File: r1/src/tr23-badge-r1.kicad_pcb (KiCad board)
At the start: 4 copper layers, 111.2 x 142.3 mm, 249 parts, among them J1 532610271, J2 USB-C-12, J3 USB-A-10mm-flangeless, J4 AFC07-S40ECA-00, J5 PJ-320D, J6 2x03-socket-2.54-through-board, J7 TF-15x15, J8 DNP, Q1 MMBT3904-TP, Q2 MMBT3904-TP, Q3 MMBT3904-TP, Q4 DMG2305UX-13, Q5 DMG2305UX-13, Q6 AP2302B, SW1 REV_TACT, SW10 REV_TACT, SW11 REV_TACT, SW12 REV_TACT, SW13 REV_TACT, SW14 REV_TACT, SW15 REV_TACT, SW16 REV_TACT, SW17 REV_TACT, SW18 REV_TACT, SW19 REV_TACT, SW2 REV_TACT, SW20 REV_TACT, SW21 REV_TACT, SW22 REV_TACT, SW23 REV_TACT, SW24 REV_TACT, SW25 REV_TACT, SW26 REV_TACT, SW27 REV_TACT, SW28 REV_TACT, SW29 REV_TACT, SW3 REV_TACT, SW30 REV_TACT, SW31 REV_TACT, SW32 REV_TACT, SW33 REV_TACT, SW34 REV_TACT, SW4 REV_TACT, SW5 REV_TACT, SW6 REV_TACT, SW7 REV_TACT, SW8 REV_TACT, SW9 REV_TACT, U1 MCP73831T-2ACI_OT, U2 AP2114H-3_3TRG1, U3 CP2102N-A01-GQFN24, U4 PCM5100APW, U5 PAM8908, U6 PCA9555PW, U7 PCA9555PW, U8 PCA9555PW, U9 CC1200, Y1 32.768kHz, Y2 40Mhz

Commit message: Position audio sectoin
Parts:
- C39, C40: moved to B.Cu
- moved C39 109.1 mm to (17.2, -86.0)
- moved Q6 72.5 mm to (-8.66, -104.1)
- moved C40 70.7 mm to (-21.2, -86.0)
- moved C19 33.2 mm to (-22.4, -109.2), turned to -90 degrees
- moved C13 32.5 mm to (-22.7, -114.6)
- moved C14 31.7 mm to (-16.9, -117.8)
- moved C17 31.7 mm to (-15.7, -118.4)
- moved C15 31.7 mm to (-18.2, -118.4)
- moved C16 31.7 mm to (-20.5, -117.7)
- moved C20 31.7 mm to (-20.1, -107.6)
- moved C22 31.7 mm to (-13.3, -112.3)
- moved C18 31.7 mm to (-21.4, -107.9)
- moved C23 31.7 mm to (-13.3, -110.8)
- moved C24 31.7 mm to (-13.3, -113.8)
- moved U4 31.7 mm to (-18.5, -113.0)
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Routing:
- net /SCL: track 11.6 -> 68.5 mm, vias 3 -> 4
- net /SDA: track 11.4 -> 67.3 mm, vias 4 -> 5
- net /I2S_SD: track 0.00 -> 21.7 mm, vias 0 -> 2
- net /I2S_WS: track 3.26 -> 23.6 mm, vias 0 -> 2
- net +3.3V: track 56.8 -> 67.1 mm, vias 17 -> 19
- net /audio/DAC_OUTL: track 0.00 -> 6.84 mm
- net /audio/DAC_OUTR: track 0.00 -> 5.16 mm
- net Net-(U5-INR-): track 0.00 -> 2.36 mm
- net Net-(U5-INL-): track 0.00 -> 2.30 mm
- net /I2S_SCK: track 0.00 -> 2.13 mm, vias 0 -> 1
- net Net-(U4-CAPP): track 0.00 -> 1.98 mm
- net Net-(U4-VNEG): track 0.00 -> 1.95 mm
- net Net-(U4-CAPM): track 0.00 -> 1.87 mm
- net /AMP_GAIN0: track 0.00 -> 1.76 mm, vias 0 -> 1
- net /audio/OUTR: track 0.00 -> 1.65 mm, vias 0 -> 1
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
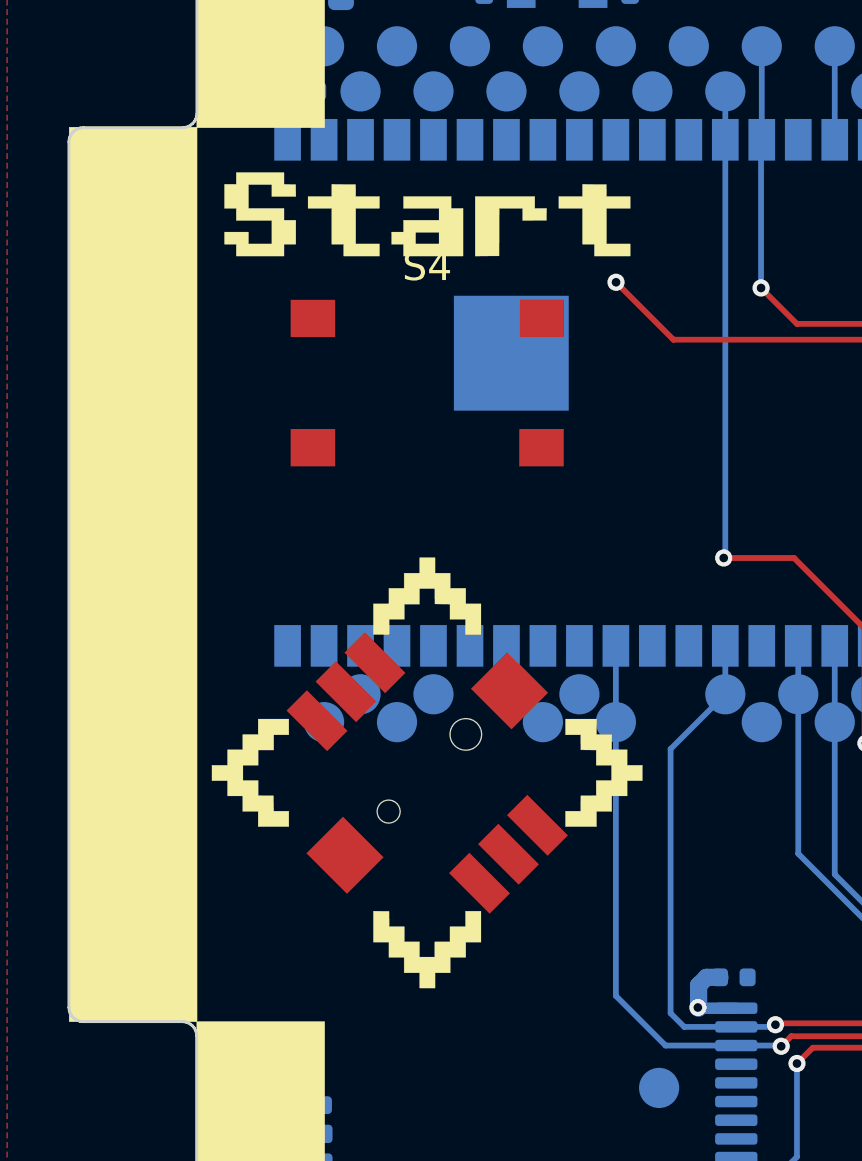
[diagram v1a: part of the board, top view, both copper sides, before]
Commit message: Tweak position of nav and A buttons, and update silk to match
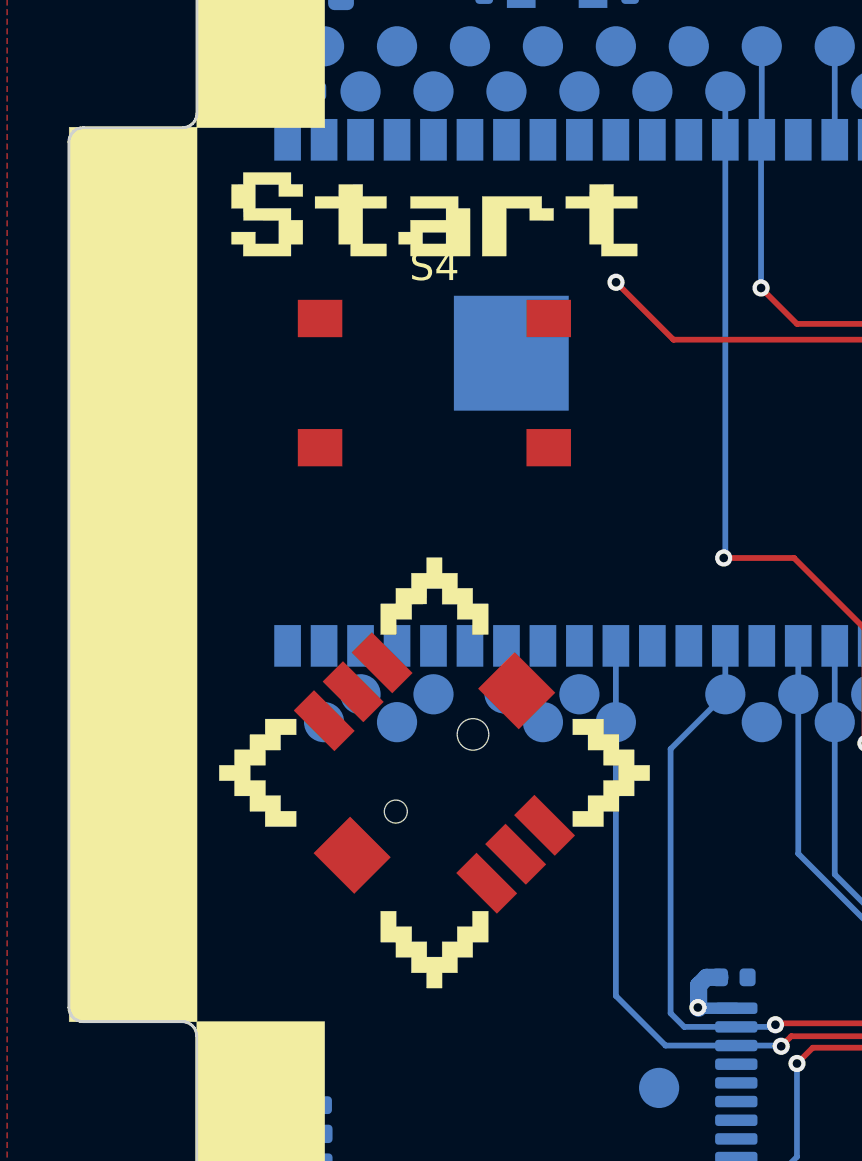
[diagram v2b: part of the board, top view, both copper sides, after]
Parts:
- moved S4 0.25 mm to (-42.9, -106.7)
- moved S5 0.25 mm to (-42.9, -93.2)

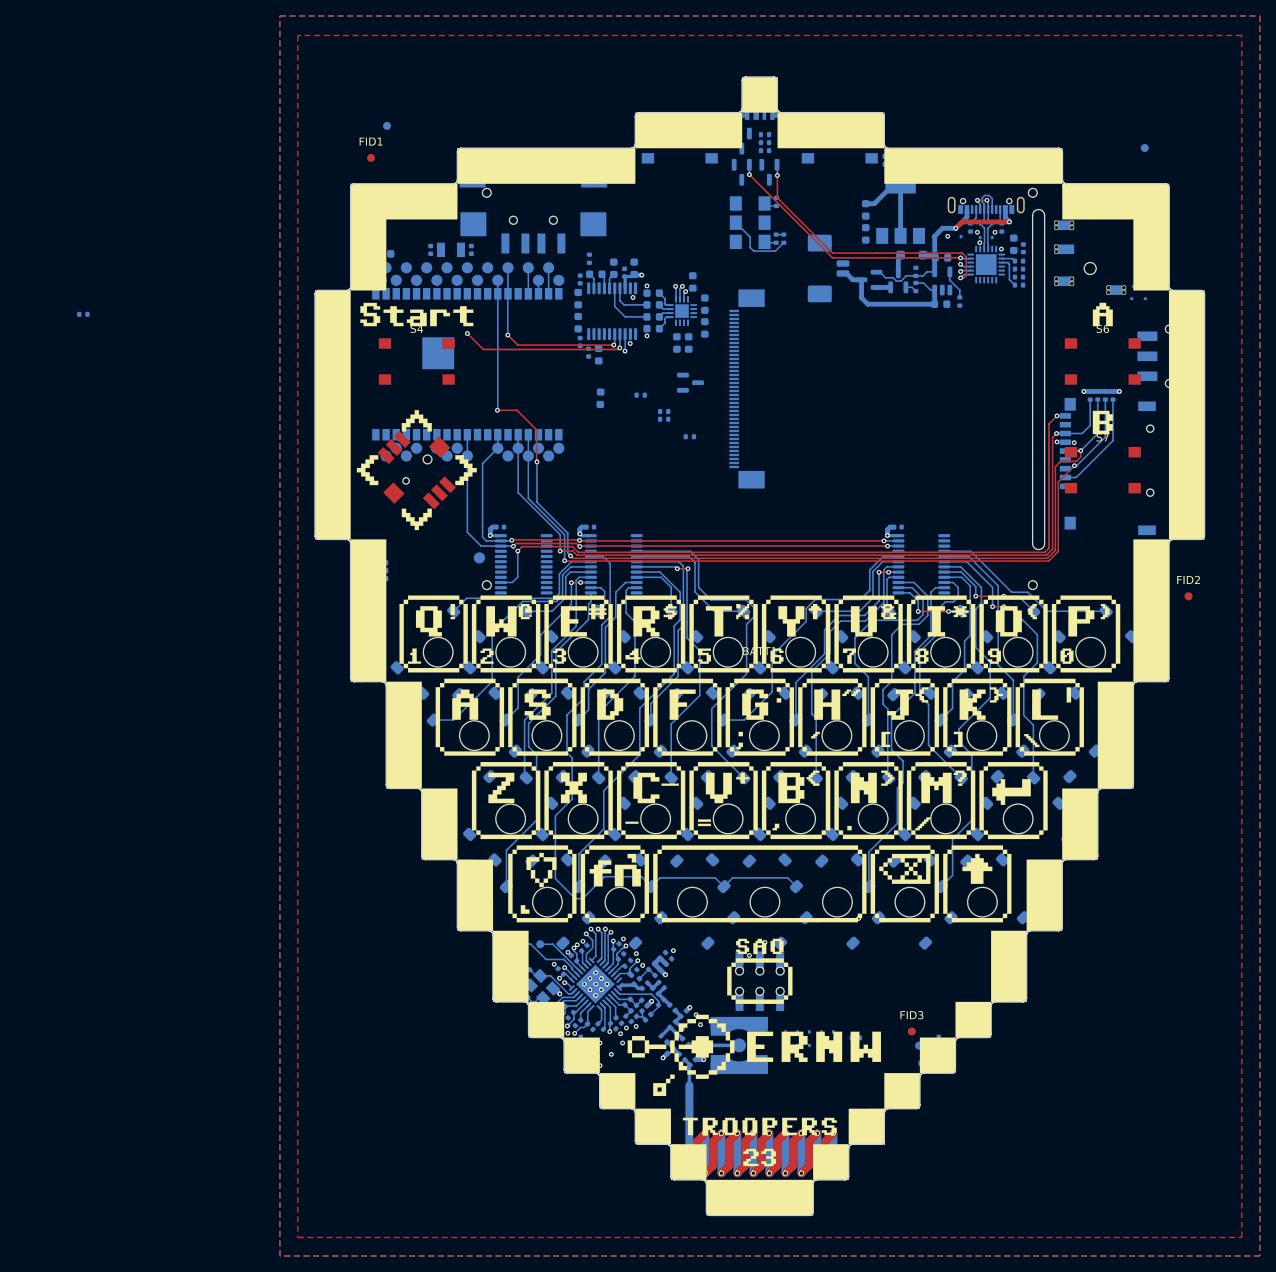
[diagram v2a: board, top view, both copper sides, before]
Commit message: Fix some DRC violations, remove footprint silk text.
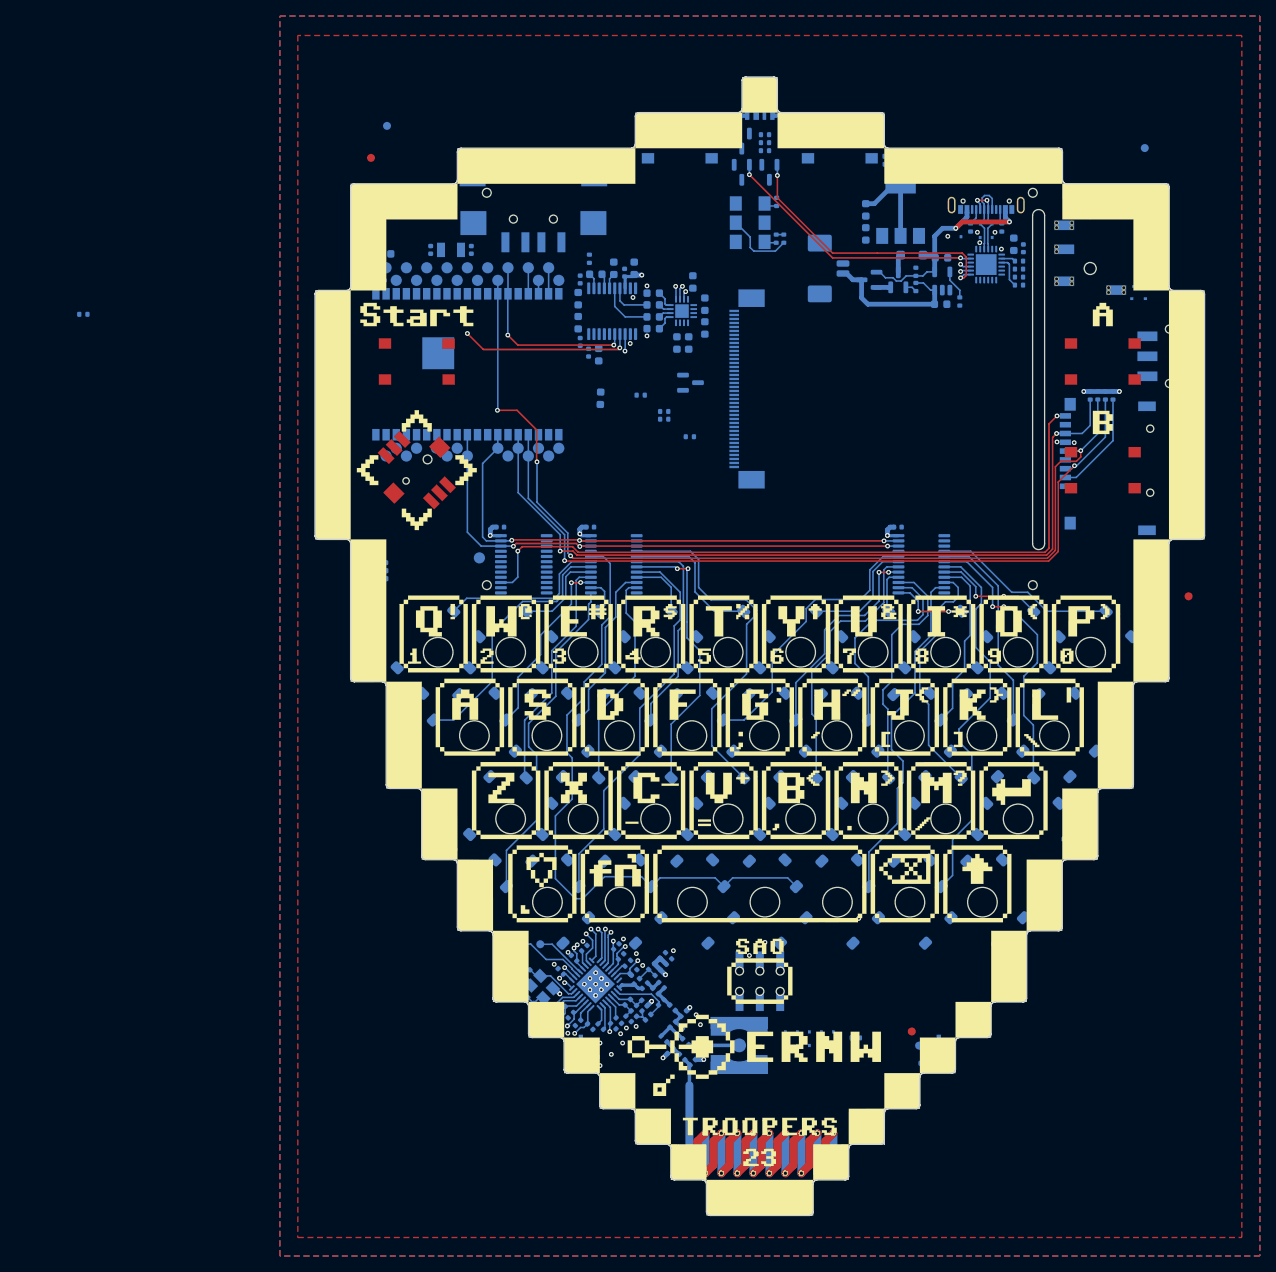
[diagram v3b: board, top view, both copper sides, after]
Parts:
- moved J3 0.15 mm to (-28.3, -124.5)

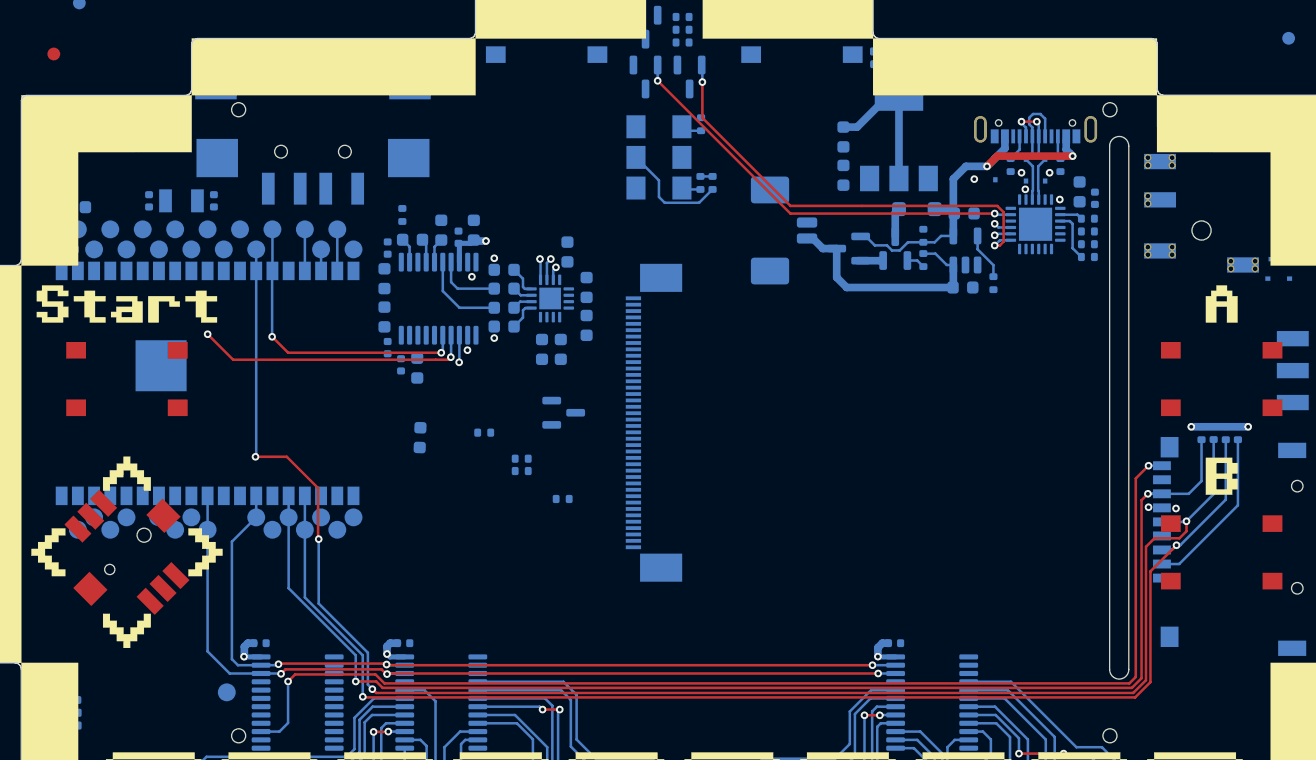
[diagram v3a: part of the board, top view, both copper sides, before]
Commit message: Display routed
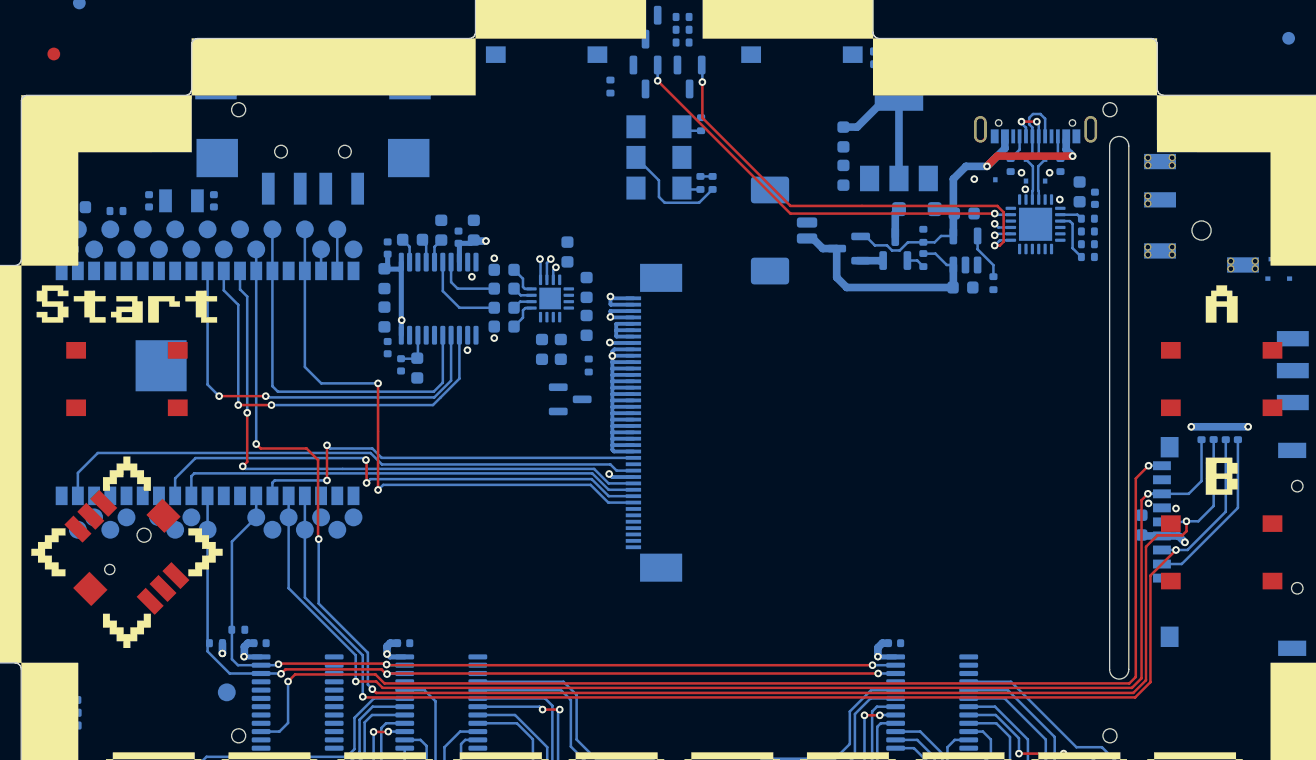
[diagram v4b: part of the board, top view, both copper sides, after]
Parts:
- moved C37 56.9 mm to (36.6, -95.3), turned to 90 degrees
- moved R6 28.9 mm to (-5.00, -129.7), turned to -90 degrees
- moved R5 28.0 mm to (-35.9, -86.0), turned to 180 degrees
- moved R4 25.4 mm to (-34.1, -87.1), turned to 180 degrees
- moved R26 22.4 mm to (-43.7, -119.9), turned to 0 degrees
- moved R32 10.7 mm to (-6.70, -107.8), turned to -90 degrees
- moved Q6 1.17 mm to (-8.15, -105.2)
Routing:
- net /~{DC}: track 0.00 -> 46.8 mm, vias 0 -> 2
- net /MOSI: track 4.45 -> 51.0 mm
- net /FSYNC: track 3.26 -> 46.1 mm, vias 0 -> 2
- net /~{DISP_CS}: track 0.00 -> 40.4 mm, vias 0 -> 2
- net GND: track 10.5 -> 50.5 mm, vias 44 -> 46
- net /SCK: track 4.38 -> 41.2 mm
- net /~{RESET}: track 0.00 -> 32.5 mm, vias 0 -> 2
- net /I2S_SCK: track 2.13 -> 32.6 mm, vias 1 -> 2
- net +3.3V: track 67.0 -> 87.7 mm, vias 19 -> 25
- net /I2S_SD: track 21.7 -> 32.5 mm
- net /I2S_WS: track 23.6 -> 29.8 mm, vias 2 -> 0
- net Net-(J4-Pin_34): track 0.00 -> 5.03 mm
- net /audio/LDO0: track 0.00 -> 3.11 mm
- net /SD_CLK: track 125.0 -> 126.1 mm
